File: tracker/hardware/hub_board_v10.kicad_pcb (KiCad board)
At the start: 2 copper layers, 72 x 80 mm, 28 parts, among them U1 U1, U2 U2, U3 U3, U5 U5, U6 U6, U7 U7

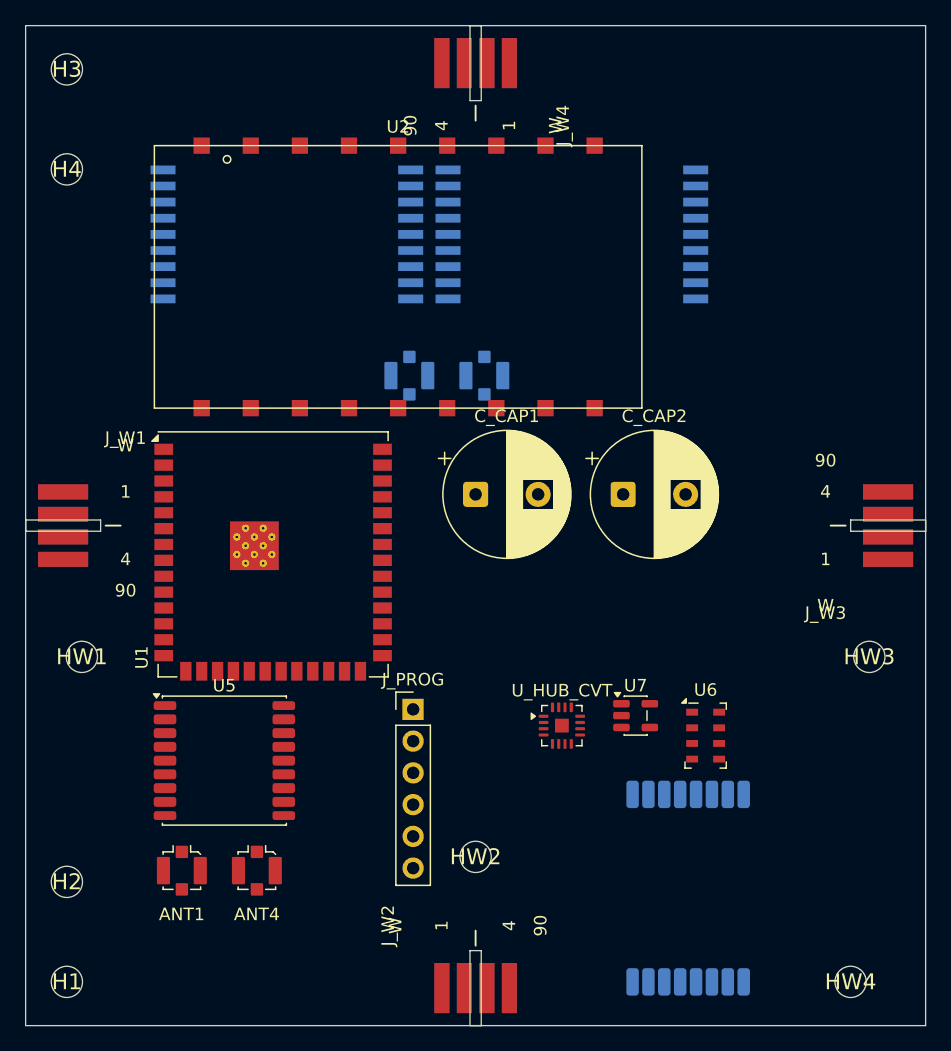
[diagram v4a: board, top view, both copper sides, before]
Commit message: fix(v10): ANT2 clear of U2.13 + router now self-validates ISOLATION (B23/B24)
B23 -- ANT2's GND shield tab (pad 2, back) overlapped U2.13 /F33_CS_N (front) by
0.25 x 0.05mm: a real cross-side pad short. ANT2 moved 0.5mm south (30.7, 28.0) ->
(30.7, 27.5), verified against U2.13 AND against every cross-side pad on the board (0
overlaps). CROSS-SIDE PAD SHORTS: 1 -> 0.

CORRECTION TO MY OWN EARLIER CLAIM: ANT2's three pads numbered "2" are the U.FL
connector's THREE GND SHIELD LEGS, all GND -- standard for this part, NOT the
duplicate-pad-number defect class I reported. That claim was wrong and is retracted here.

GATE CORRECTED: check_cross_side_collision.py had been failing on COURTYARD overlap
across sides, which is NOT a defect -- parts on opposite faces sit at different Z, and
sharing X-Y area is exactly what two-sided population MEANS (ADR-118). It produced 5
FALSE positives, e.g. U2 (F33, 39x21mm per the vendor datasheet -- its courtyard is
CORRECT, my earlier "oversized courtyard" claim was also wrong) over U3/U_C on the
opposite face. The gate now fails ONLY on PAD-vs-PAD overlap across sides (a real short
through the board) and prints courtyard sharing as INFO. This is what caught U1/U_E28.

B24 -- the router now validates its own output against ISOLATION. Measured after the
placement fix: 5 violations, all a track routed through another net's via or track
(/F33_BUSY through /F33_RESET_N's via at -0.350mm; /SPI2_MISO x via). The router marked
routed copper as a grid OBSTACLE but never checked its own output against it. validate_plan
now applies the check_lane_isolation rules in memory -- track-vs-track (same layer),
track-vs-via, via-vs-track, via-vs-via, all >= CLEAR between copper edges -- and records
each ACCEPTED net's copper so later nets are validated against it.

MEASURED RESULT (all EIGHT gates):
  routed 15 nets, failed 22 (reported, never forced), rails deferred to pours
  board geometry 0 · hole clearance 0 · lane clearance 0 · lane integrity 0
  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
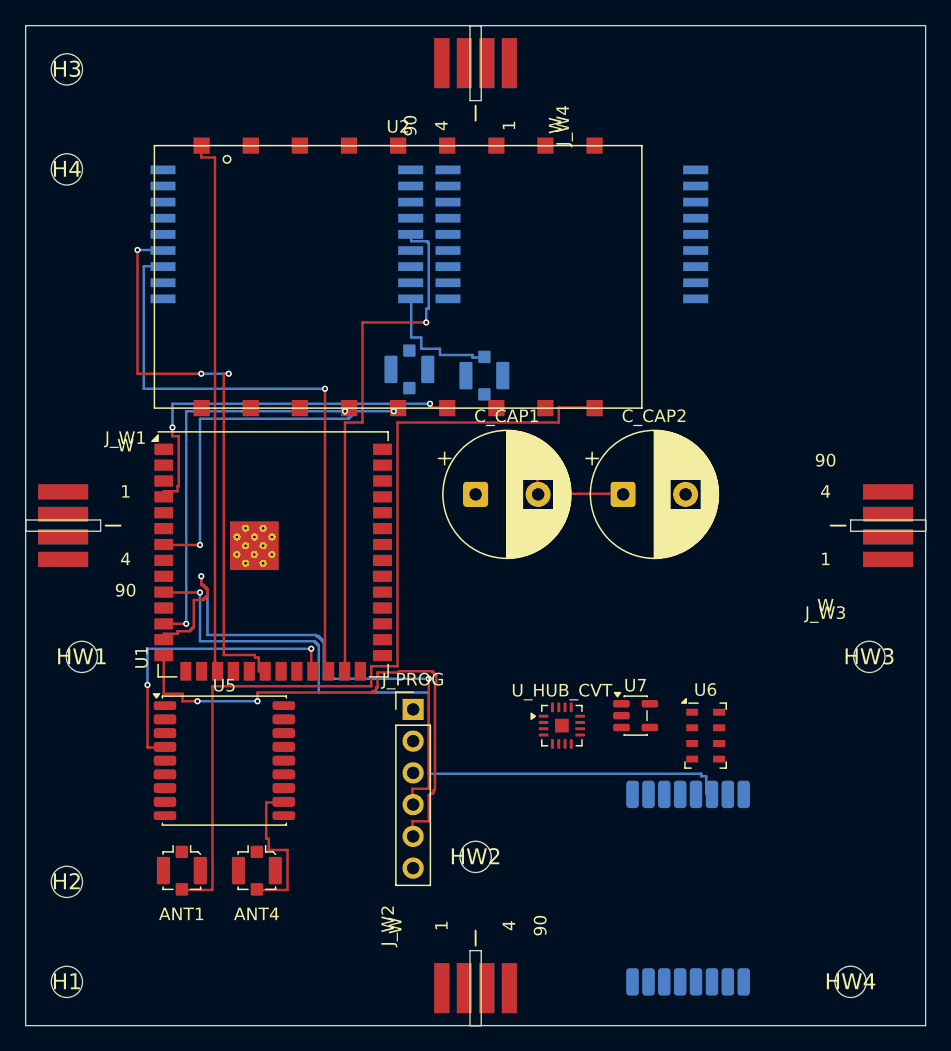
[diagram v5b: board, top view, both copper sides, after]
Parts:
- moved ANT2 0.50 mm to (30.7, 27.5)
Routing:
- net /ANT1_433_TX: track 0.00 -> 71.7 mm
- net /E28_CS_N: track 0.00 -> 60.0 mm, vias 0 -> 1
- net /U3_BUSY: track 0.00 -> 48.7 mm, vias 0 -> 1
- net /USB_DN: track 0.00 -> 46.9 mm, vias 0 -> 2
- net /U3_CS_N: track 0.00 -> 46.7 mm, vias 0 -> 3
- net /F33_IRQ: track 0.00 -> 43.4 mm
- net /U3_RESET_N: track 0.00 -> 43.0 mm, vias 0 -> 1
- net /USB_DP: track 0.00 -> 43.0 mm, vias 0 -> 2
- net /F33_BUSY: track 0.00 -> 32.1 mm, vias 0 -> 2
- net /SPI2_SCK: track 0.00 -> 31.5 mm, vias 0 -> 2
- net /F33_CS_N: track 0.00 -> 29.7 mm, vias 0 -> 2
- net /GNSS_PPS: track 0.00 -> 24.3 mm, vias 0 -> 2
- net /ANT4_GNSS_L1: track 0.00 -> 12.6 mm
- net /ANT3_2G4_RX: track 0.00 -> 10.6 mm
- net /SCAP_MID: track 0.00 -> 9.80 mm

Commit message: perf(v10): A* 16x faster (B26-B28); net-ordering knob added -- but routed count DROPPED, stated honestly
WHY: the earlier "15 nets routed, 8 gates zero" run was only possible because the A* took
~5s/net; a 3-order comparison exceeded 500s and I could not tell whether the placement fix
or the ordering was responsible for anything. Making the search fast was necessary to even
MEASURE routing quality. It cost routed nets, and that trade is recorded here rather than
hidden.

B26 -- the A* heuristic was UNWEIGHTED. With BEND_COST and VIA_COST in the path cost, an
  unweighted Manhattan heuristic expanded nearly every reachable cell: measured 5.07s for
  ONE 2-pad net (300-cell path on a 722x802 grid). Now weight 2.0. This trades optimality
  for speed: we do not need the SHORTEST path, only a LEGAL one -- validate_plan gates every
  candidate afterwards.
B27 -- flat arrays instead of dicts keyed by (i,j,l) tuples; a tuple was allocated per node.
  Also fixed TWO BUGS introduced by that rewrite, both caught by measurement:
    * path reconstruction used nx as the (i,j) stride while idx() used ny -> scrambled paths.
    * a CLOSED node could be re-parented, creating a parent CYCLE: the reconstruction then
      looped forever (observed: >300s with zero output, no traceback).
  A hard MAX_EXP cap now returns None (net reported unrouted) instead of hanging.
B28 -- precomputed via feasibility ONCE per grid. The seek re-checked a (2r+1)^2 ~ 225-cell
  free disc at EVERY expansion: 330,050 disc calls = 2.0s of the 5.07s. Now an O(1) lookup.
  MEASURED: 5.07s -> 0.31s per net.

B25 -- net ordering is now selectable (--order constrained|alpha|longest|reverse).
  Default "constrained" = fewest pads, then smallest extent (standard PCB practice: route
  the nets with least freedom first).

MEASURED, same board, dry-run, four orderings:
  constrained  10 nets
  alpha         9 nets
  longest       8 nets
  (before these three changes, alpha reached 15)

HONEST READING: the fast searc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
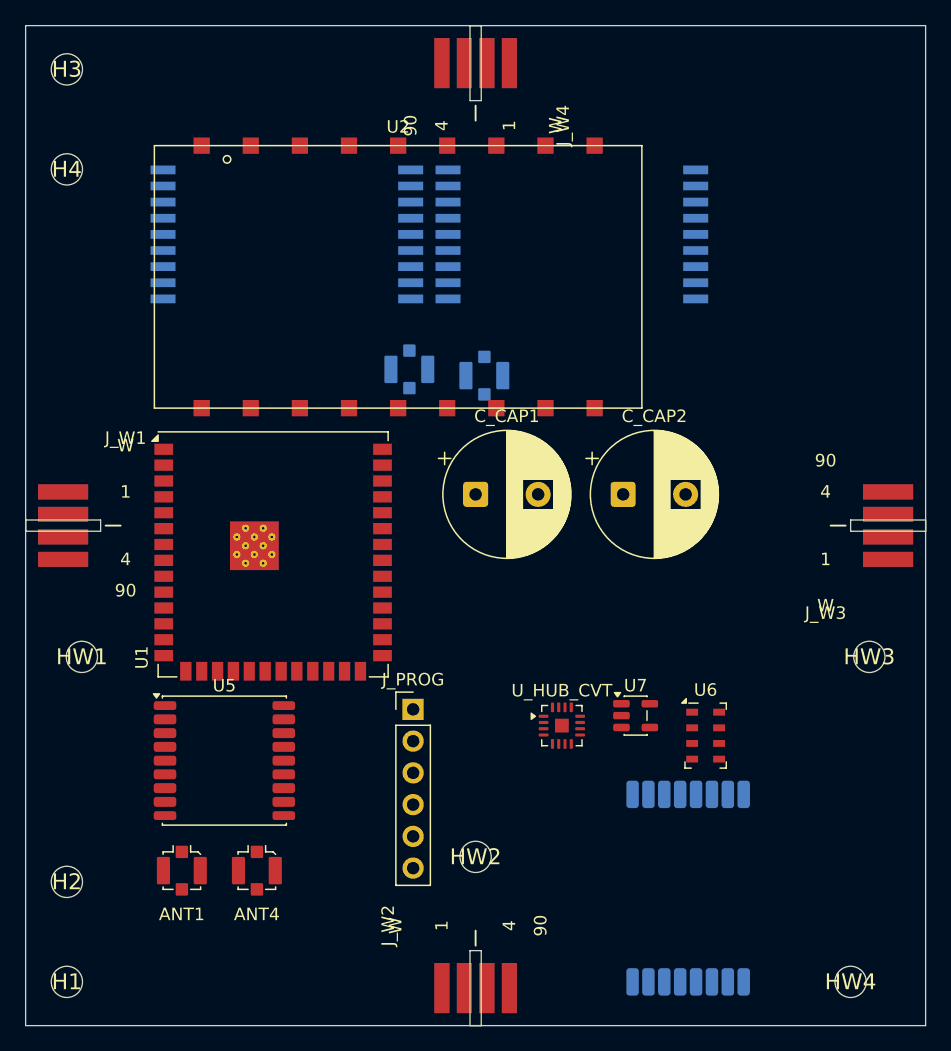
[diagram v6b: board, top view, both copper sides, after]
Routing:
- net /ANT1_433_TX: track 71.7 -> 0.00 mm
- net /E28_CS_N: track 60.0 -> 0.00 mm, vias 1 -> 0
- net /U3_BUSY: track 48.7 -> 0.00 mm, vias 1 -> 0
- net /USB_DN: track 46.9 -> 0.00 mm, vias 2 -> 0
- net /U3_CS_N: track 46.7 -> 0.00 mm, vias 3 -> 0
- net /F33_IRQ: track 43.4 -> 0.00 mm
- net /U3_RESET_N: track 43.0 -> 0.00 mm, vias 1 -> 0
- net /USB_DP: track 43.0 -> 0.00 mm, vias 2 -> 0
- net /F33_BUSY: track 32.1 -> 0.00 mm, vias 2 -> 0
- net /SPI2_SCK: track 31.5 -> 0.00 mm, vias 2 -> 0
- net /F33_CS_N: track 29.7 -> 0.00 mm, vias 2 -> 0
- net /GNSS_PPS: track 24.3 -> 0.00 mm, vias 2 -> 0
- net /ANT4_GNSS_L1: track 12.6 -> 0.00 mm
- net /ANT3_2G4_RX: track 10.6 -> 0.00 mm
- net /SCAP_MID: track 9.80 -> 0.00 mm
